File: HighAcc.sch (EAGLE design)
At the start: 22 parts, among them J401 M12PTH, U101 BMP180, U401 7432, U501 L3G4200D, U601 ADXL345, U801 5883

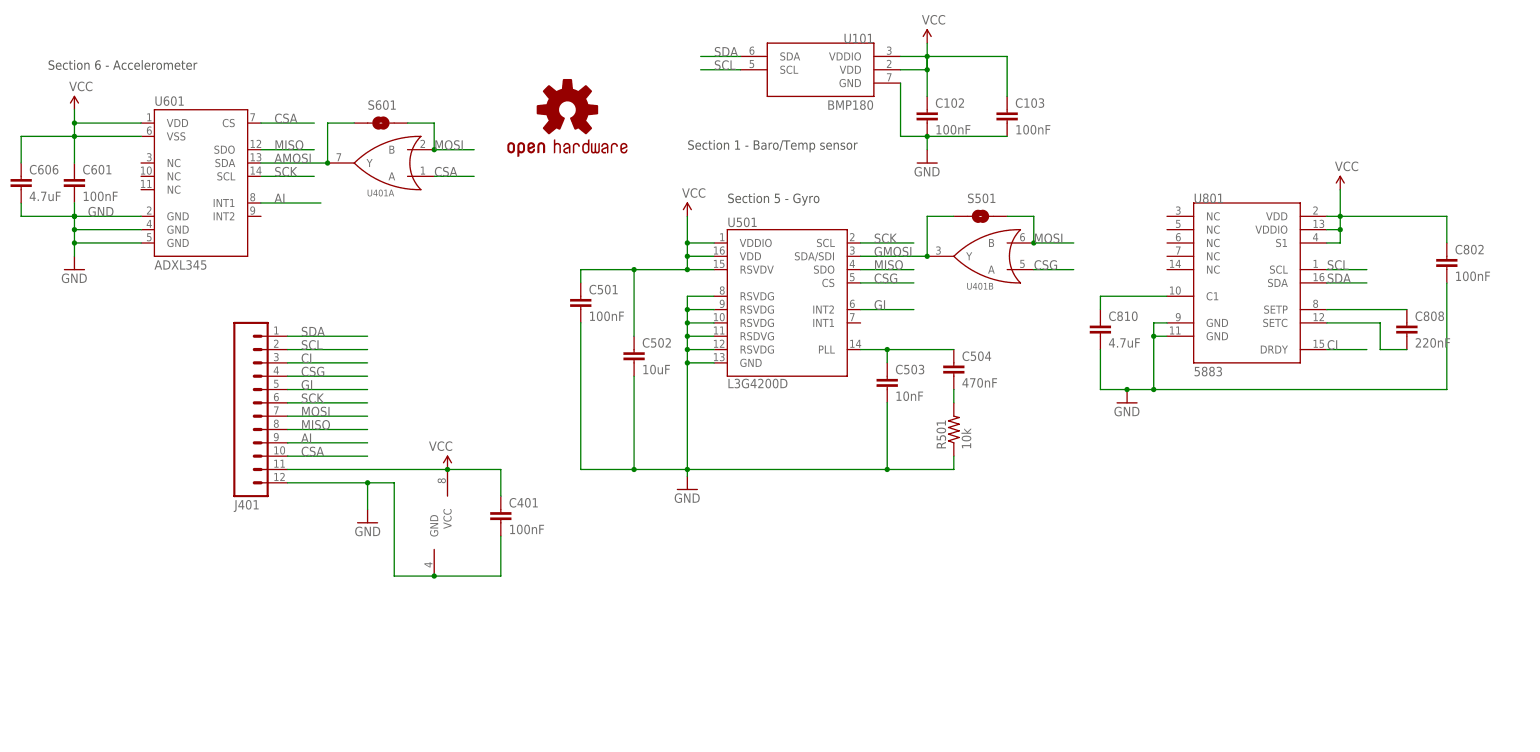
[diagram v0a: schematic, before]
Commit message: Merged Mio's KwanSystems.lbr, updated all eagle files to use it.
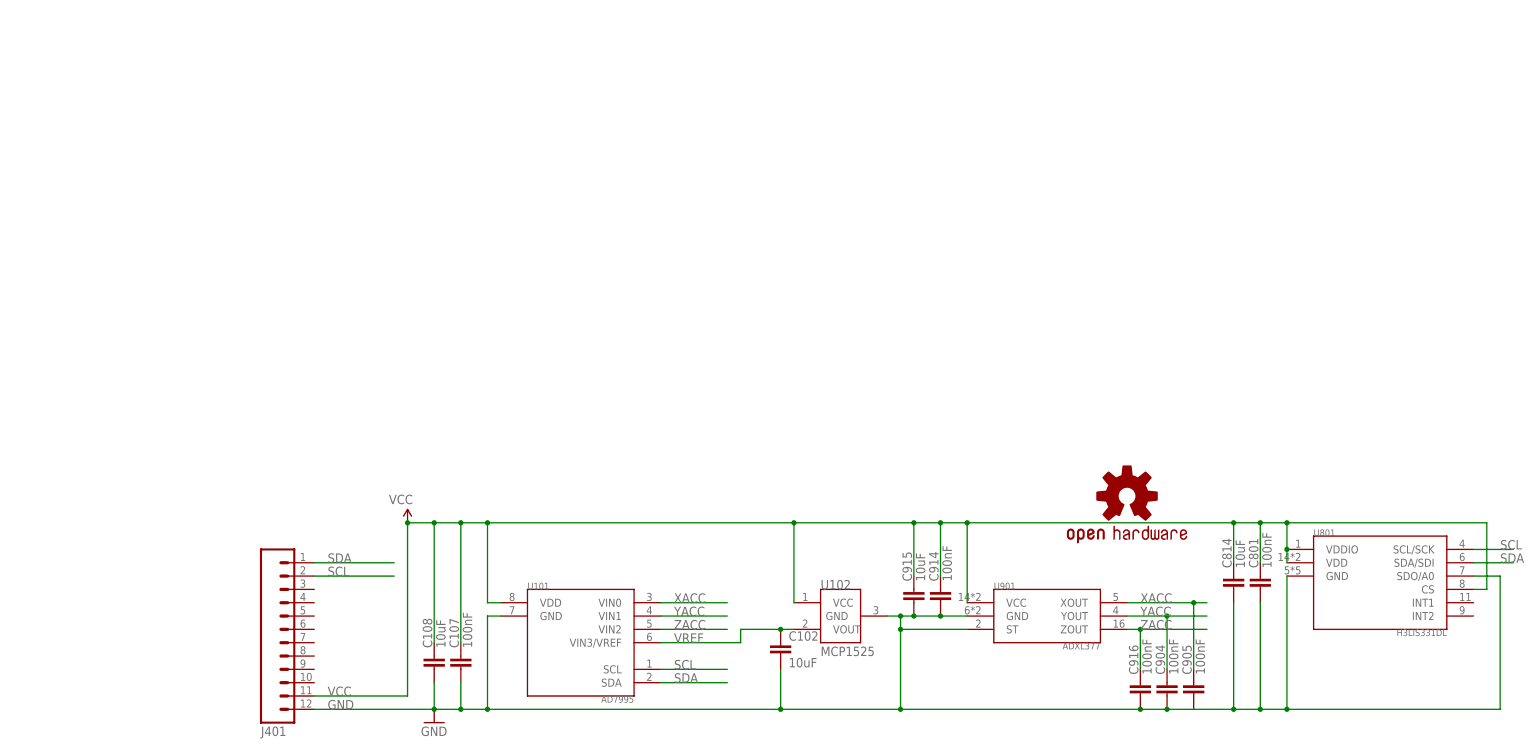
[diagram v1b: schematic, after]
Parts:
- removed C103, C401, C501, C601, C802: 100nF, SparkFun:CAP0603-CAP
- removed C502: 10uF, SparkFun:CAP0603-CAP
- removed C503: 10nF, SparkFun:CAP0603-CAP
- removed C504: 470nF, SparkFun:CAP0603-CAP
- removed C606, C810: 4.7uF, SparkFun:CAP0603-CAP
- removed C808: 220nF, SparkFun:CAP0603-CAP
- removed R501: 10k, SparkFun:RESISTOR0603-RES
- removed S501, S601: SOLDERJUMPERNO, SparkFun:SOLDERJUMPERNO
- removed U401: 7432, KwanSystems:SN74LVC2G32
- removed U501: L3G4200D, SparkFun:L3G4200D
- removed U601: ADXL345, SparkFun:ADXL345
- added C107, C801, C904, C905, C914, C916: 100nF, SparkFun:CAP0603-CAP
- added C108, C814, C915: 10uF, SparkFun:CAP0603-CAP
- added U102: MCP1525, KwanSystems:MCP1525
- added U901: ADXL377, KwanSystems:ADXL377
- C102: value 100nF -> 10uF; DIGIKEY 445-1316-1-ND -> 445-7486-1-ND
- U101: value BMP180 -> AD7995; device KwanSystems:BMP180 -> KwanSystems:AD799X; DIGIKEY 828-1027-1-ND -> (none)
- U801: value 5883 -> H3LIS331DL; device SparkFun:HMC5883LSMD -> KwanSystems:H3LIS331DL; DIGIKEY 342-1082-1-ND -> (none)
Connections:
- removed net AI: J401.9, U601.INT1
- removed net AMOSI: S601.1, U401A.Y, U601.SDA
- removed net CI: J401.3, U801.DRDY
- removed net CSA: J401.10, U401A.A, U601.CS
- removed net CSG: J401.4, U401B.A, U501.CS
- removed net GI: J401.5, U501.INT2
- removed net GMOSI: S501.1, U401B.Y, U501.SDA/SDI
- removed net MISO: J401.8, U501.SDO, U601.SDO
- removed net MOSI: J401.7, S501.2, S601.2, U401A.B, U401B.B
- removed net N$1: C503.1, C504.1, U501.PLL
- removed net N$14: C808.1, U801.SETP
- removed net N$15: C808.2, U801.SETC
- removed net N$16: C810.1, U801.C1
- removed net N$2: C504.2, R501.2
- removed net SCK: J401.6, U501.SCL, U601.SCL
- new net VREF: C102.1, U101.VIN3/VREF, U102.VOUT
- new net XACC: C905.1, U101.VIN0, U901.XOUT
- new net YACC: C904.1, U101.VIN1, U901.YOUT
- new net ZACC: C916.1, U101.VIN2, U901.ZOUT
- net GND: now also C107.2, C108.2, C801.2, C814.2, C904.2, C905.2, C914.2, C915.2, C916.2, U102.GND, U801.GND, U801.SDO/A0, U901.GND, U901.ST; no longer C103.2, C401.2, C501.2, C502.2, C503.2, C601.2, C606.2, C802.2, C810.2, R501.1, U401PWR.GND, U501.GND, U501.RSDVG@3, U501.RSVDG@0, U501.RSVDG@1, U501.RSVDG@2, U501.RSVDG@4, U601.GND@2, U601.GND@4, U601.GND@5, U801.GND@1, U801.GND@2
- net SCL: now also U801.SCL/SCK; no longer U801.SCL
- net SDA: now also U801.SDA/SDI; no longer U801.SDA
- net VCC: now also C107.1, C108.1, C801.1, C814.1, C914.1, C915.1, U102.VCC, U801.CS, U901.VCC; no longer C102.1, C103.1, C401.1, C501.1, C502.1, C601.1, C606.1, C802.1, U101.VDDIO, U401PWR.VCC, U501.RSVDV@0, U501.VDD, U501.VDDIO, U601.VDD, U601.VSS, U801.S1
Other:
- note removed: "Section 1 - Baro/Temp sensor"
- note removed: "Section 5 - Gyro"
- note removed: "Section 6 - Accelerometer"
- moved on the sheet: C102, J401

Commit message: RocketometerMPU sent to Laen
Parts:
- added SJ1, SJ2, SJ3, SJ4: SOLDERJUMPERNO, SparkFun-Passives:SOLDERJUMPERNO
- U101: DIGIKEY (none) -> AD7995YRJZ-1500RL7CT-ND
- U102: DIGIKEY (none) -> MCP1525T-I/TTCT-ND
- U801: DIGIKEY (none) -> $NOPART
- U901: DIGIKEY (none) -> ADXL377BCPZ-RL7CT-ND
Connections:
- new net N$1: J401.3, SJ1.1
- new net N$2: J401.4, SJ2.1
- new net N$3: J401.5, SJ3.1
- new net N$4: J401.9, SJ4.1
- net VREF: now also SJ4.2, U101.VIN2; no longer U101.VIN3/VREF
- net XACC: now also SJ1.2
- net YACC: now also SJ2.2
- net ZACC: now also SJ3.2, U101.VIN3/VREF; no longer U101.VIN2
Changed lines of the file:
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@@
 <attribute name="DIGIKEY" value="$NOPART"/>
 </part>
-<part name="U101" library="KwanSystems" deviceset="AD799X" device="" value="AD7995"/>
-<part name="U901" library="KwanSystems" deviceset="ADXL377" device=""/>
-<part name="U801" library="KwanSystems" deviceset="H3LIS331DL" device=""/>
-<part name="U102" library="KwanSystems" deviceset="MCP1525" device=""/>
+<part name="U101" library="KwanSystems" deviceset="AD799X" device="" value="AD7995">
+<attribute name="DIGIKEY" value="AD7995YRJZ-1500RL7CT-ND"/>
+</part>
+<part name="U901" library="KwanSystems" deviceset="ADXL377" device="">
+<attribute name="DIGIKEY" value="ADXL377BCPZ-RL7CT-ND"/>
+</part>
+<part name="U801" library="KwanSystems" deviceset="H3LIS331DL" device="">
+<attribute name="DIGIKEY" value="$NOPART"/>
+</part>
+<part name="U102" library="KwanSystems" deviceset="MCP1525" device="">
+<attribute name="DIGIKEY" value="MCP1525T-I/TTCT-ND"/>
+</part>
 <part name="C102" library="SparkFun" deviceset="CAP" device="0603-CAP" value="10uF">
 <attribute name="DIGIKEY" value="445-7486-1-ND"/>
@@
 <part name="C801" library="SparkFun" deviceset="CAP" device="0603-CAP" value="100nF">
 <attribute name="DIGIKEY" value="445-1316-1-ND"/>
+</part>
+<part name="SJ1" library="SparkFun-Passives" deviceset="SOLDERJUMPER" device="NO">
+<attribute name="DIGIKEY" value="$NOPART"/>
+</part>
+<part name="SJ2" library="SparkFun-Passives" deviceset="SOLDERJUMPER" device="NO">
+<attribute name="DIGIKEY" value="$NOPART"/>
+</part>
+<part name="SJ3" library="SparkFun-Passives" deviceset="SOLDERJUMPER" device="NO">
+<attribute name="DIGIKEY" value="$NOPART"/>
+</part>
+<part name="SJ4" library="SparkFun-Passives" deviceset="SOLDERJUMPER" device="NO">
+<attribute name="DIGIKEY" value="$NOPART"/>
 </part>
 </parts>
@@
 <attribute name="DIGIKEY" x="223.52" y="154.94" size="1.778" layer="96" display="off"/>
 </instance>
-<instance part="U101" gate="G$1" x="119.38" y="127"/>
-<instance part="U901" gate="G$1" x="208.28" y="132.08"/>
-<instance part="U801" gate="G$1" x="271.78" y="139.7"/>
-<instance part="U102" gate="G$1" x="170.18" y="132.08"/>
+<instance part="U101" gate="G$1" x="119.38" y="127">
+<attribute name="DIGIKEY" x="119.38" y="127" size="1.778" layer="96" display="off"/>
+</instance>
+<instance part="U901" gate="G$1" x="208.28" y="132.08">
+<attribute name="DIGIKEY" x="208.28" y="132.08" size="1.778" layer="96" display="off"/>
+</instance>
+<instance part="U801" gate="G$1" x="271.78" y="139.7">
+<attribute name="DIGIKEY" x="271.78" y="139.7" size="1.778" layer="96" display="off"/>
+</instance>
+<instance part="U102" gate="G$1" x="170.18" y="132.08">
+<attribute name="DIGIKEY" x="170.18" y="132.08" size="1.778" layer="96" display="off"/>
+</instance>
 <instance part="C102" gate="G$1" x="157.48" y="124.46">
 <attribute name="DIGIKEY" x="157.48" y="124.46" size="1.778" layer="96" display="off"/>
@@
 <attribute name="NAME" x="248.539" y="141.224" size="1.778" layer="95" rot="R90"/>
 <attribute name="VALUE" x="251.079" y="141.224" size="1.778" layer="96" rot="R90"/>
+</instance>
+<instance part="SJ1" gate="1" x="76.2" y="137.16" smashed="yes">
+<attribute name="NAME" x="68.58" y="137.16" size="1.778" layer="95"/>
+<attribute name="DIGIKEY" x="76.2" y="137.16" size="1.778" layer="96" display="off"/>
+</instance>
+<instance part="SJ2" gate="1" x="76.2" y="134.62" smashed="yes">
+<attribute name="NAME" x="68.58" y="134.62" size="1.778" layer="95"/>
+<attribute name="DIGIKEY" x="76.2" y="134.62" size="1.778" layer="96" display="off"/>
+</instance>
+<instance part="SJ3" gate="1" x="76.2" y="132.08" smashed="yes">
+<attribute name="NAME" x="68.58" y="132.08" size="1.778" layer="95"/>
+<attribute name="DIGIKEY" x="76.2" y="132.08" size="1.778" layer="96" display="off"/>
+</instance>
+<instance part="SJ4" gate="1" x="76.2" y="121.92" smashed="yes">
+<attribute name="NAME" x="68.58" y="121.92" size="1.778" layer="95"/>
+<attribute name="DIGIKEY" x="76.2" y="121.92" size="1.778" layer="96" display="off"/>
 </instance>
 </instances>
@@
 <pinref part="C102" gate="G$1" pin="1"/>
 <wire x1="157.48" y1="129.54" x2="160.02" y2="129.54" width="0.1524" layer="91"/>
-<wire x1="157.48" y1="129.54" x2="149.86" y2="129.54" width="0.1524" layer="91"/>
-<wire x1="149.86" y1="129.54" x2="149.86" y2="127" width="0.1524" layer="91"/>
-<pinref part="U101" gate="G$1" pin="VIN3/VREF"/>
-<wire x1="149.86" y1="127" x2="134.62" y2="127" width="0.1524" layer="91"/>
-<label x="137.16" y="127" size="1.778" layer="95"/>
+<pinref part="U101" gate="G$1" pin="VIN2"/>
+<wire x1="157.48" y1="129.54" x2="134.62" y2="129.54" width="0.1524" layer="91"/>
+<label x="137.16" y="129.54" size="1.778" layer="95"/>
 <junction x="157.48" y="129.54"/>
+</segment>
+<segment>
+<pinref part="SJ4" gate="1" pin="2"/>
+<wire x1="81.28" y1="121.92" x2="83.82" y2="121.92" width="0.1524" layer="91"/>
+<label x="81.28" y="121.92" size="1.778" layer="95"/>
 </segment>
 </net>
@@
 </segment>
 <segment>
-<pinref part="U101" gate="G$1" pin="VIN2"/>
-<wire x1="134.62" y1="129.54" x2="147.32" y2="129.54" width="0.1524" layer="91"/>
-<label x="137.16" y="129.54" size="1.778" layer="95"/>
+<pinref part="U101" gate="G$1" pin="VIN3/VREF"/>
+<wire x1="134.62" y1="127" x2="147.32" y2="127" width="0.1524" layer="91"/>
+<label x="137.16" y="127" size="1.778" layer="95"/>
+</segment>
+<segment>
+<pinref part="SJ3" gate="1" pin="2"/>
+<wire x1="81.28" y1="132.08" x2="83.82" y2="132.08" width="0.1524" layer="91"/>
+<label x="81.28" y="132.08" size="1.778" layer="95"/>
 </segment>
 </net>
@@
 <label x="137.16" y="132.08" size="1.778" layer="95"/>
 </segment>
+<segment>
+<pinref part="SJ2" gate="1" pin="2"/>
+<wire x1="81.28" y1="134.62" x2="83.82" y2="134.62" width="0.1524" layer="91"/>
+<label x="81.28" y="134.62" size="1.778" layer="95"/>
+</segment>
 </net>
 <net name="XACC" class="0">
@@
 <label x="137.16" y="134.62" size="1.778" layer="95"/>
 </segment>
-</net>
+<segment>
+<pinref part="SJ1" gate="1" pin="2"/>
+<wire x1="81.28" y1="137.16" x2="83.82" y2="137.16" width="0.1524" layer="91"/>
+<label x="81.28" y="137.16" size="1.778" layer="95"/>
+</segment>
+</net>
+<net name="N$1" class="0">
+<segment>
+<pinref part="J401" gate="G$1" pin="3"/>
+<pinref part="SJ1" gate="1" pin="1"/>
+<wire x1="71.12" y1="137.16" x2="68.58" y2="137.16" width="0.1524" layer="91"/>
+</segment>
+</net>
+<net name="N$2" class="0">
+<segment>
+<pinref part="J401" gate="G$1" pin="4"/>
+<pinref part="SJ2" gate="1" pin="1"/>
+<wire x1="71.12" y1="134.62" x2="68.58" y2="134.62" width="0.1524" layer="91"/>
+</segment>
+</net>
+<net name="N$3" class="0">
+<segment>
+<pinref part="J401" gate="G$1" pin="5"/>
+<pinref part="SJ3" gate="1" pin="1"/>
+<wire x1="71.12" y1="132.08" x2="68.58" y2="132.08" width="0.1524" layer="91"/>
+</segment>
+</net>
+<net name="N$4" class="0">
+<segment>
+<pinref part="J401" gate="G$1" pin="9"/>
+<wire x1="68.58" y1="121.92" x2="71.12" y2="121.92" width="0.1524" layer="91"/>
+<pinref part="SJ4" gate="1" pin="1"/>
+</segment>
+</net>
